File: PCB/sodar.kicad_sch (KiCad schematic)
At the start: 2 parts, among them U1 TC78H621FNG

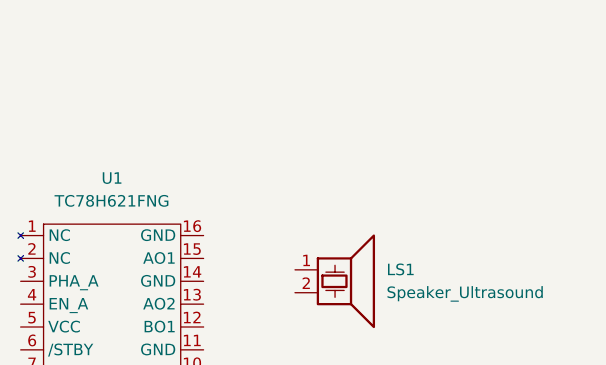
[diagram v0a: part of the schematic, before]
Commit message: Added Receiver & LED components
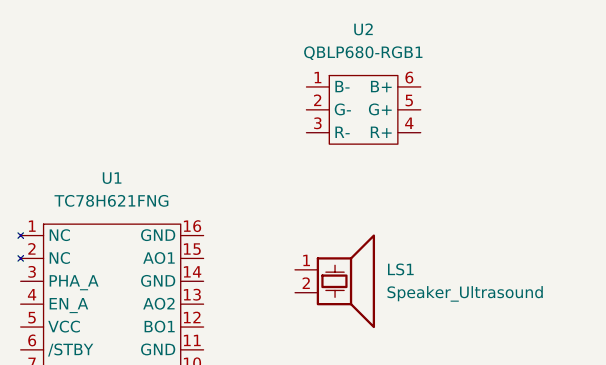
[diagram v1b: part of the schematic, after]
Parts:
- added U2: QBLP680-RGB1, footprints:QBLP680-RGB1, symbol symbols:QBLP680-RGB1
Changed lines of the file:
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@@
+	)
+	(symbol
+		(lib_id "symbols:QBLP680-RGB1")
+		(at 71.12 34.29 0)
+		(unit 1)
+		(exclude_from_sim no)
+		(in_bom yes)
+		(on_board yes)
+		(dnp no)
+		(fields_autoplaced yes)
+		(property "Reference" "U2"
+			(at 71.12 31.75 0)
+			(effects
+				(font
+					(size 1.27 1.27)
+				)
+			)
+		)
+		(property "Value" "QBLP680-RGB1"
+			(at 71.12 34.29 0)
+			(effects
+				(font
+					(size 1.27 1.27)
+				)
+			)
+		)
+		(property "Footprint" "footprints:QBLP680-RGB1"
+			(at 71.12 34.29 0)
+			(effects
+				(font
+					(size 1.27 1.27)
+				)
+				(hide yes)
+			)
+		)
+		(property "Datasheet" ""
+			(at 71.12 34.29 0)
+			(effects
+				(font
+					(size 1.27 1.27)
+				)
+				(hide yes)
+			)
+		)
+		(property "Description" ""
+			(at 71.12 34.29 0)
+			(effects
+				(font
+					(size 1.27 1.27)
+				)
+				(hide yes)
+			)
+		)
+		(pin "1"
+		)
+		(pin "3"
+		)
+		(pin "5"
+		)
+		(pin "6"
+		)
+		(pin "2"
+		)
+		(pin "4"
+		)
+		(instances
+			(project ""
+				(path "/f620949f-55f1-4ffa-a6f4-2a6276be8919"
+					(reference "U2")
+					(unit 1)
+				)
+			)
+		)
 	)
 	(symbol

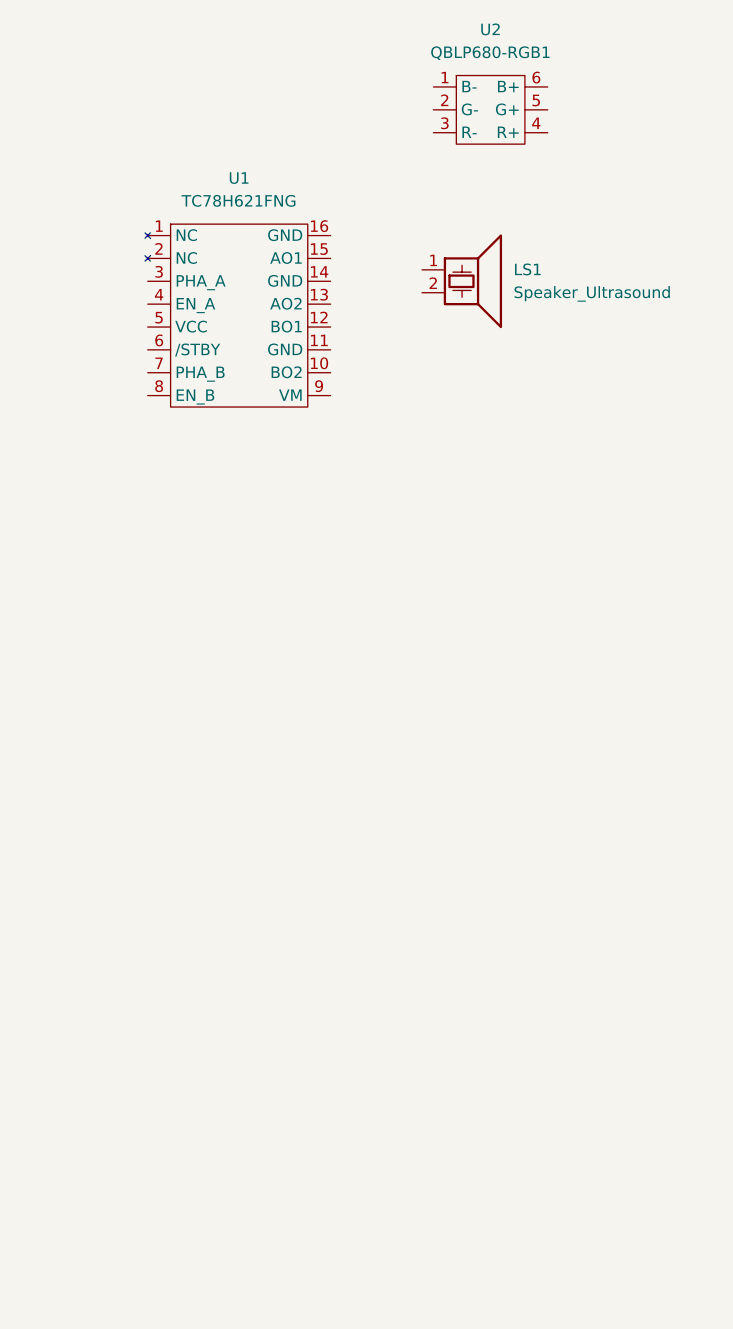
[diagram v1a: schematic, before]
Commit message: Wired first driver-tansducer module
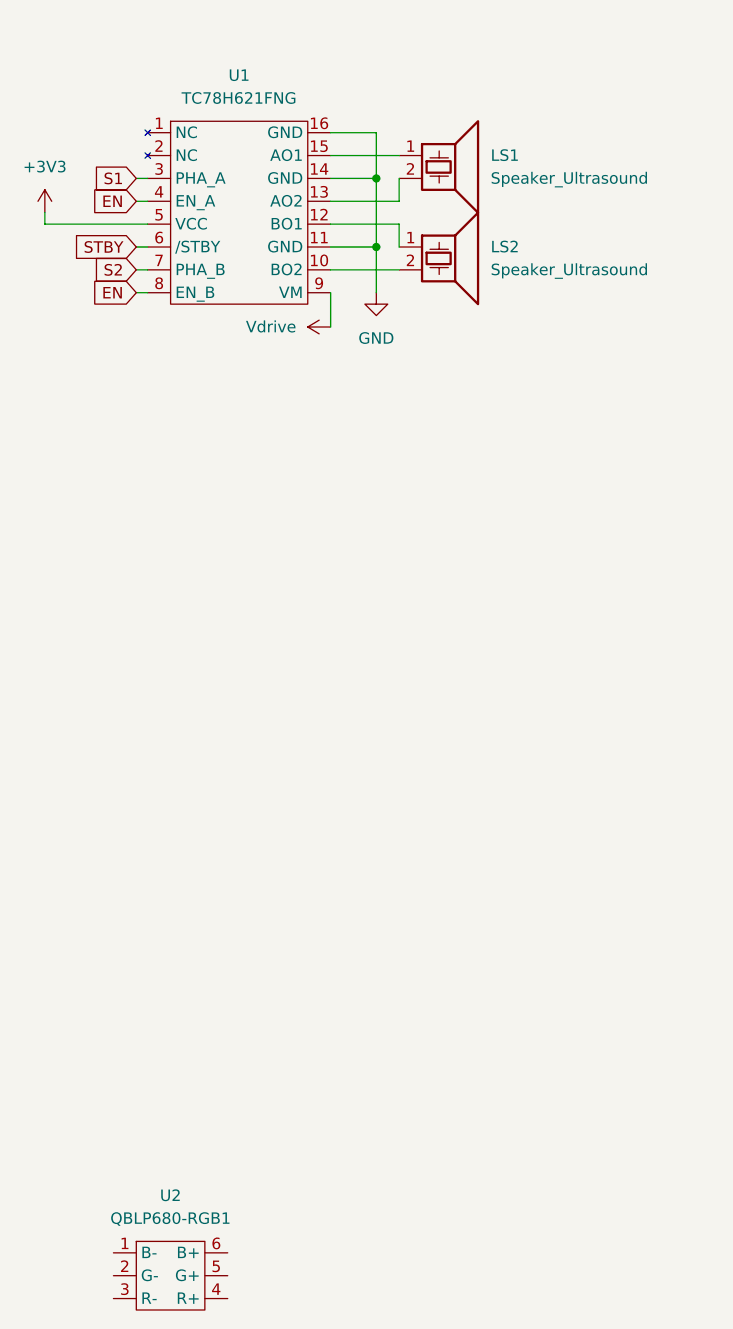
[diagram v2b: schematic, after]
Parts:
- added LS2: Speaker_Ultrasound, footprints:CUSA-T80-15-2400-TH, symbol Device:Speaker_Ultrasound
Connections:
- net at U1.10 (BO2): now also LS2.2
- net GND: now reaches U1.11 (GND)
- net GND: now also U1.14 (GND), U1.16 (GND)
- net at U1.12 (BO1): now also LS2.1
- net at U1.13 (AO2): now also LS1.2
- net at U1.15 (AO1): now also LS1.1
- net S1: now reaches U1.3 (PHA_A)
- net EN: now reaches U1.4 (EN_A)
- net EN: now also U1.8 (EN_B)
- net +3V3: now reaches U1.5 (VCC)
- net STBY: now reaches U1.6 (/STBY)
- net S2: now reaches U1.7 (PHA_B)
- net Vdrive: now reaches U1.9 (VM)
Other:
- moved on the sheet: LS1, U1, U2

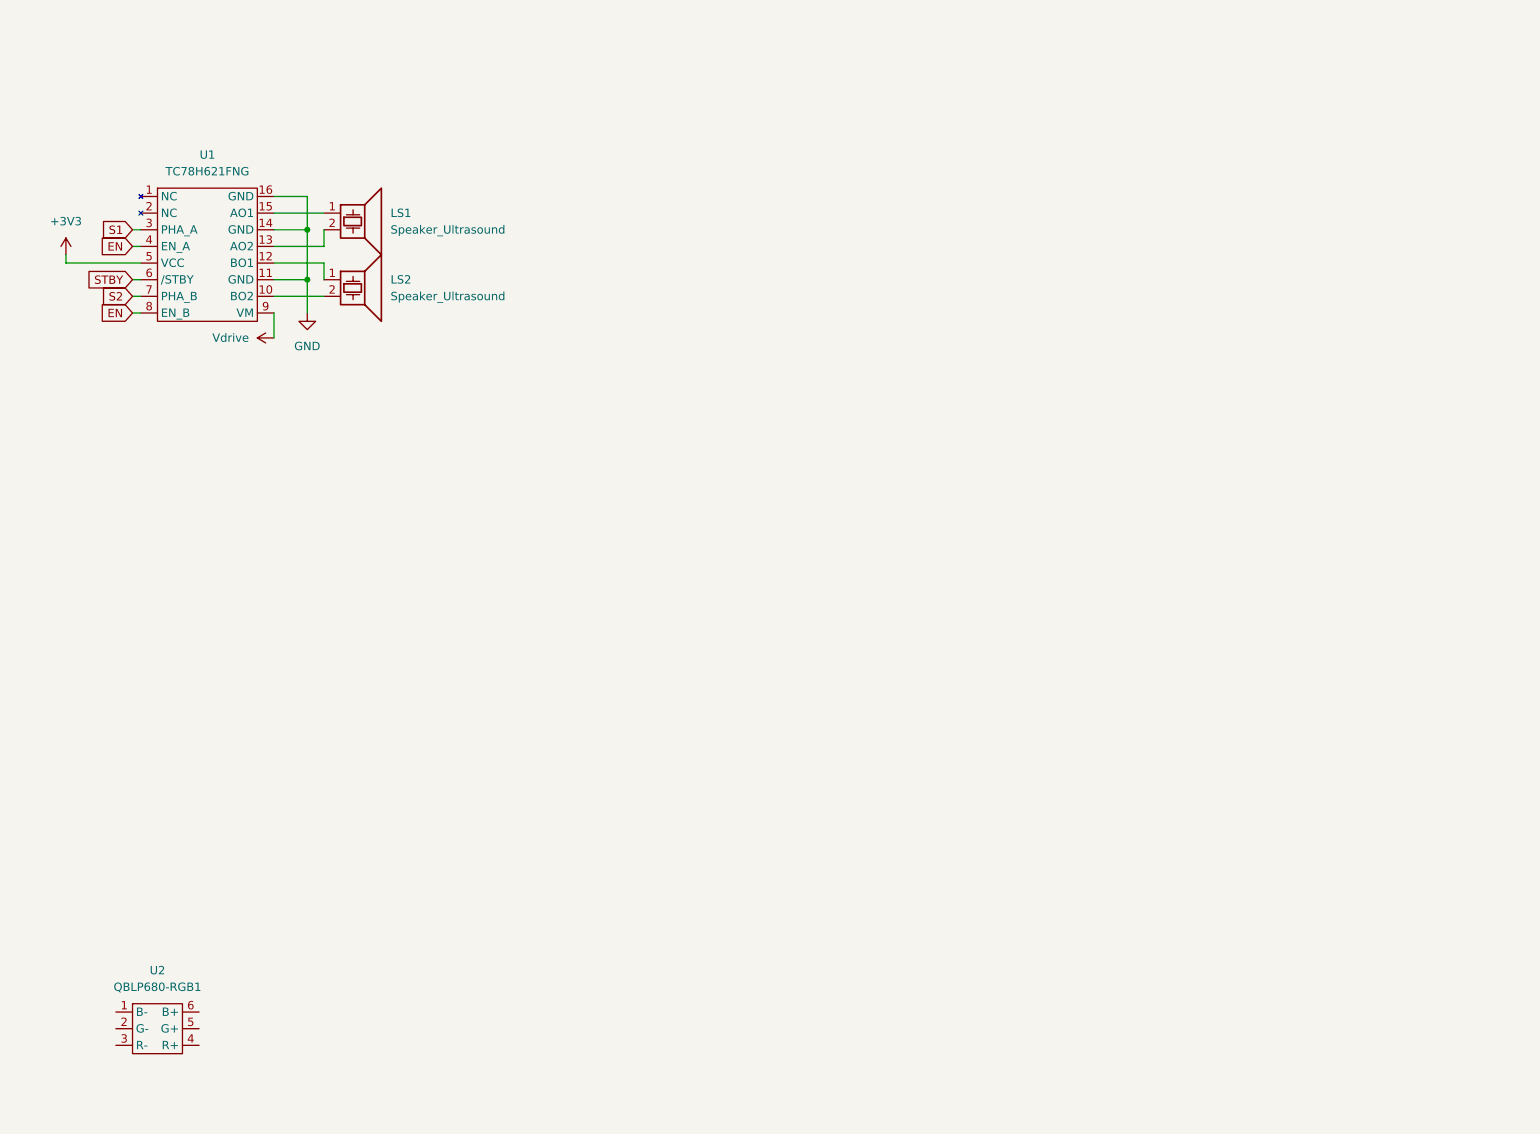
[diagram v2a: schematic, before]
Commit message: Added the remaining drivers & transducer to the schematics
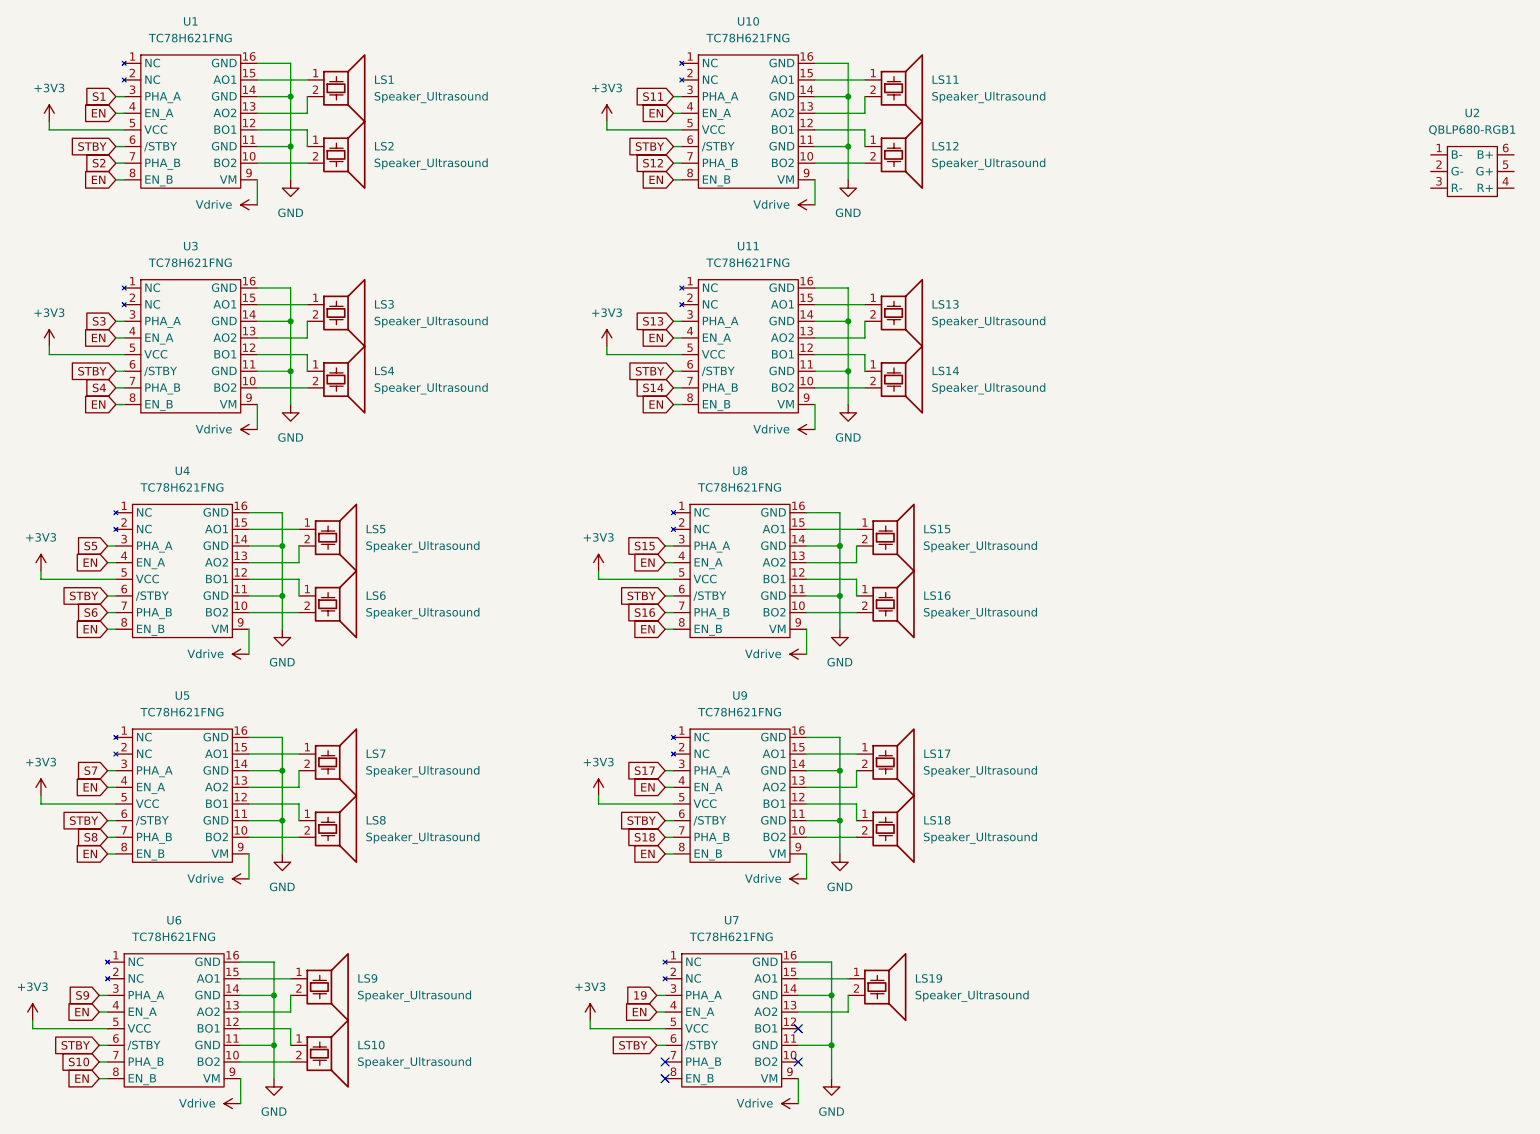
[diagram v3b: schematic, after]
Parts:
- added LS10, LS11, LS12, LS13, LS14, LS15, LS16, LS17, LS18, LS19, LS3, LS4, LS5, LS6, LS7, LS8, LS9: Speaker_Ultrasound, footprints:CUSA-T80-15-2400-TH, symbol Device:Speaker_Ultrasound
- added U10, U11, U3, U4, U5, U6, U7, U8, U9: TC78H621FNG, Package_SO:TSSOP-16_4.4x5mm_P0.65mm, symbol symbols:TC78H621FNG
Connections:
- net +3V3: now also U10.5 (VCC), U11.5 (VCC), U3.5 (VCC), U4.5 (VCC), U5.5 (VCC), U6.5 (VCC), U7.5 (VCC), U8.5 (VCC), U9.5 (VCC)
- net EN: now also U10.4 (EN_A), U10.8 (EN_B), U11.4 (EN_A), U11.8 (EN_B), U3.4 (EN_A), U3.8 (EN_B), U4.4 (EN_A), U4.8 (EN_B), U5.4 (EN_A), U5.8 (EN_B), U6.4 (EN_A), U6.8 (EN_B), U7.4 (EN_A), U8.4 (EN_A), U8.8 (EN_B), U9.4 (EN_A), U9.8 (EN_B)
- net GND: now also U10.11 (GND), U10.14 (GND), U10.16 (GND), U11.11 (GND), U11.14 (GND), U11.16 (GND), U3.11 (GND), U3.14 (GND), U3.16 (GND), U4.11 (GND), U4.14 (GND), U4.16 (GND), U5.11 (GND), U5.14 (GND), U5.16 (GND), U6.11 (GND), U6.14 (GND), U6.16 (GND), U7.11 (GND), U7.14 (GND), U7.16 (GND), U8.11 (GND), U8.14 (GND), U8.16 (GND), U9.11 (GND), U9.14 (GND), U9.16 (GND)
- net STBY: now also U10.6 (/STBY), U11.6 (/STBY), U3.6 (/STBY), U4.6 (/STBY), U5.6 (/STBY), U6.6 (/STBY), U7.6 (/STBY), U8.6 (/STBY), U9.6 (/STBY)
- net Vdrive: now also U10.9 (VM), U11.9 (VM), U3.9 (VM), U4.9 (VM), U5.9 (VM), U6.9 (VM), U7.9 (VM), U8.9 (VM), U9.9 (VM)
- new net: LS11.1, U10.15 (AO1)
- new net: LS11.2, U10.13 (AO2)
- new net: LS19.2, U7.13 (AO2)
- new net: LS19.1, U7.15 (AO1)
- new net: LS15.1, U8.15 (AO1)
- new net: LS15.2, U8.13 (AO2)
- new net: LS14.2, U11.10 (BO2)
- new net: LS14.1, U11.12 (BO1)
- new net: LS13.2, U11.13 (AO2)
- new net: LS13.1, U11.15 (AO1)
- new net: LS9.1, U6.15 (AO1)
- new net: LS9.2, U6.13 (AO2)
- new net: LS8.2, U5.10 (BO2)
- new net: LS8.1, U5.12 (BO1)
- new net: LS7.2, U5.13 (AO2)
- new net: LS7.1, U5.15 (AO1)
- new net: LS10.1, U6.12 (BO1)
- new net: LS10.2, U6.10 (BO2)
- new net: LS12.2, U10.10 (BO2)
- new net: LS12.1, U10.12 (BO1)
- new net: LS16.2, U8.10 (BO2)
- new net: LS16.1, U8.12 (BO1)
- new net: LS17.1, U9.15 (AO1)
- new net: LS17.2, U9.13 (AO2)
- new net: LS3.1, U3.15 (AO1)
- new net: LS3.2, U3.13 (AO2)
- new net: LS18.2, U9.10 (BO2)
- new net: LS18.1, U9.12 (BO1)
- new net: LS6.1, U4.12 (BO1)
- new net: LS6.2, U4.10 (BO2)
- new net: LS5.1, U4.15 (AO1)
- new net: LS5.2, U4.13 (AO2)
- new net: LS4.1, U3.12 (BO1)
- new net: LS4.2, U3.10 (BO2)
- new net 19: U7.3 (PHA_A)
- new net S10: U6.7 (PHA_B)
- new net S11: U10.3 (PHA_A)
- new net S12: U10.7 (PHA_B)
- new net S13: U11.3 (PHA_A)
- new net S14: U11.7 (PHA_B)
- new net S15: U8.3 (PHA_A)
- new net S16: U8.7 (PHA_B)
- new net S17: U9.3 (PHA_A)
- new net S18: U9.7 (PHA_B)
- new net S3: U3.3 (PHA_A)
- new net S4: U3.7 (PHA_B)
- new net S5: U4.3 (PHA_A)
- new net S6: U4.7 (PHA_B)
- new net S7: U5.3 (PHA_A)
- new net S8: U5.7 (PHA_B)
- new net S9: U6.3 (PHA_A)
- no-connect marks 0 -> 4
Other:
- moved on the sheet: LS1, LS2, U1, U2
